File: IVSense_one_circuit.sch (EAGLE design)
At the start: 10 parts

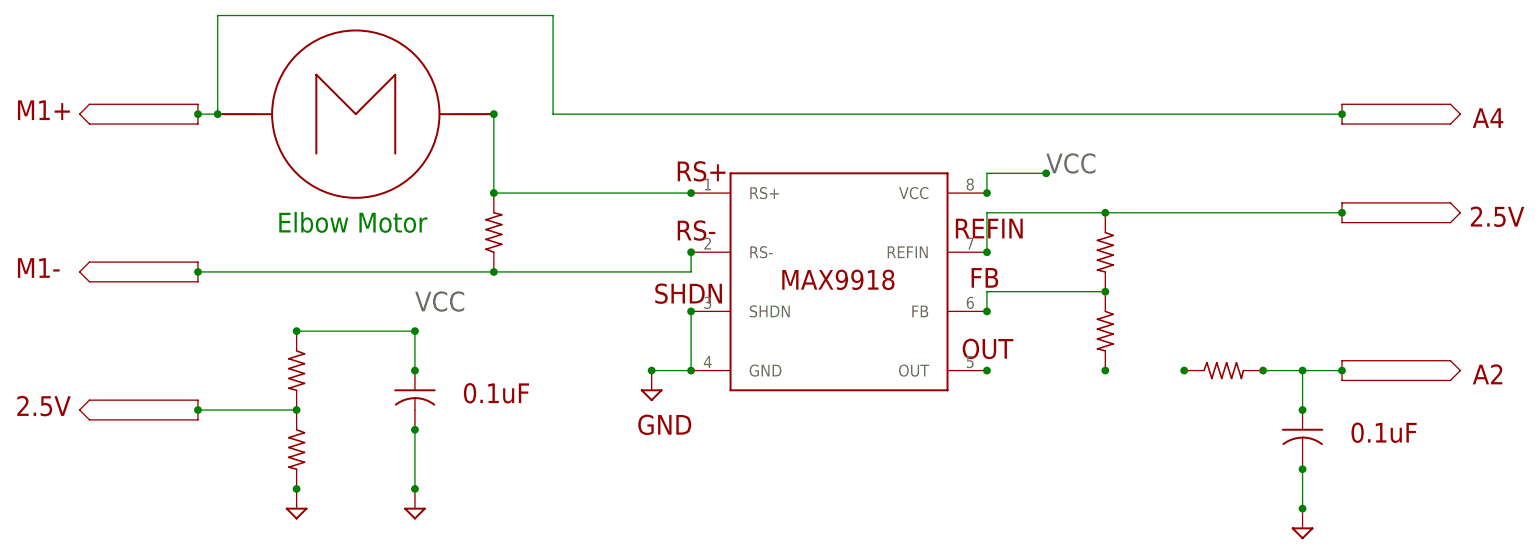
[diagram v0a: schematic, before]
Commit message: modified:   IVSense - Schematic Image (one circuit).png modified:   IVSense_one_circuit.sch
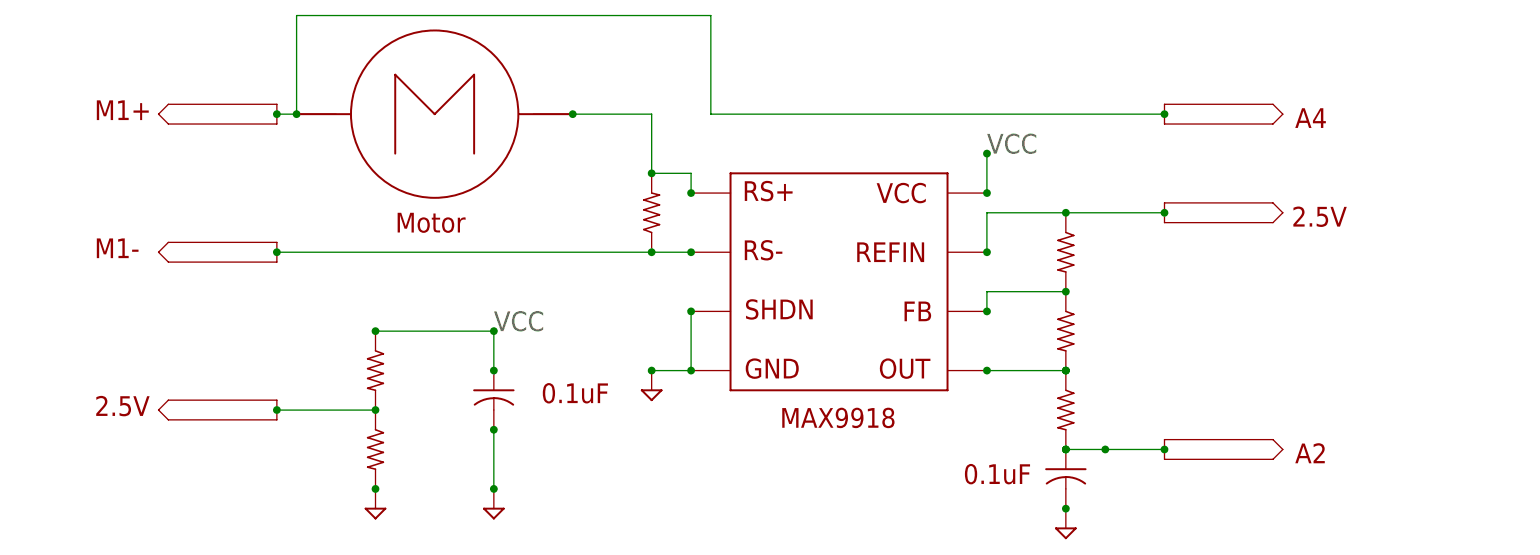
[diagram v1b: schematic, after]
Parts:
- R5, R6: value 1k -> 10k
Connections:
- removed net N$10: RF_E.1
- removed net N$13: RB.2
- removed net N$14: MAX9918.OUT
- new net N$2: MAX9918.OUT, RB.2, RF_E.1
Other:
- note added: "Motor"
- note removed: "Elbow Motor"
- note removed: "FB"
- note removed: "OUT"
- note removed: "REFIN"
- note removed: "RS+"
- note removed: "RS-"
- note removed: "SHDN"
